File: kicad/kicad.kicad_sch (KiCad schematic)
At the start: 7 parts, among them J1 Screw_Terminal_01x14, U1 Pico

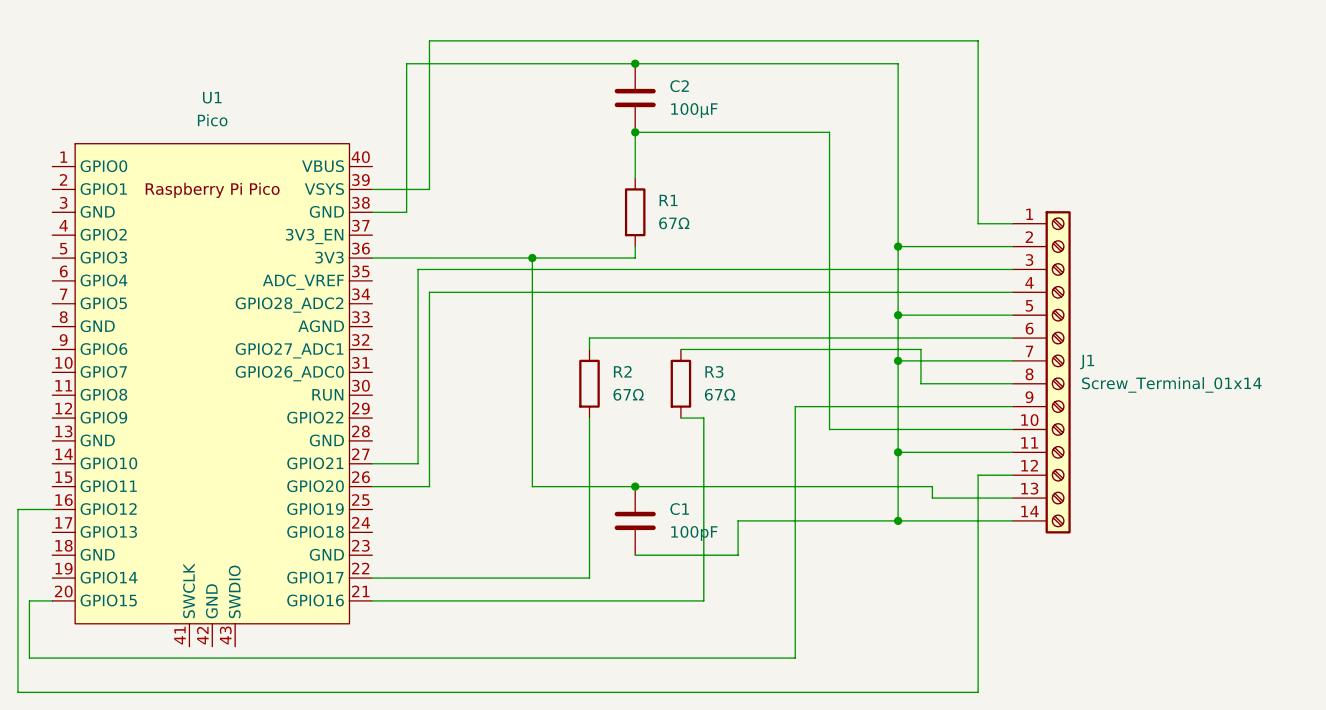
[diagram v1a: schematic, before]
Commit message: new PCB layout
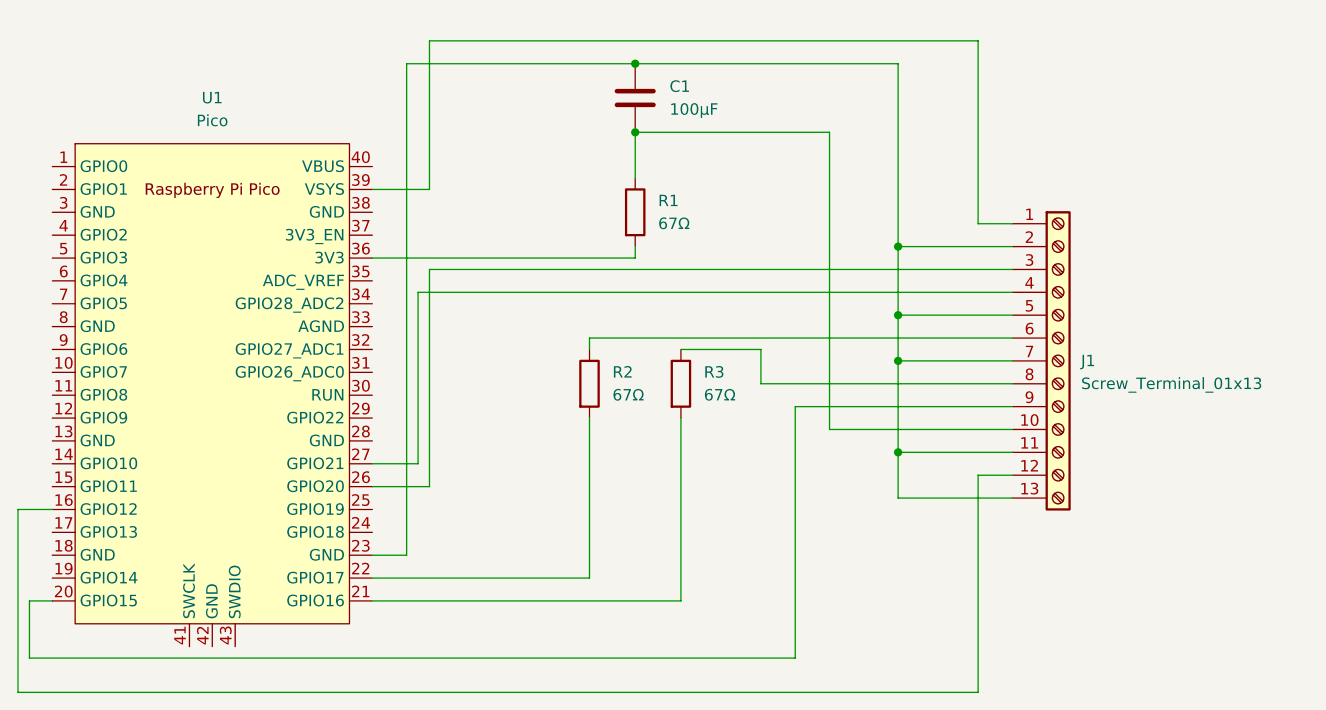
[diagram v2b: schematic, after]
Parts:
- removed C1: 100pF, Capacitor_THT:C_Disc_D7.0mm_W2.5mm_P5.00mm, symbol Device:C
- J1: value Screw_Terminal_01x14 -> Screw_Terminal_01x13
- renumbered C2 to C1
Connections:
- net at R1.2, U1.36 (3V3): no longer J1.13 (Pin_13)
- net at C1.1, J1.11 (Pin_11), J1.2 (Pin_2)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: now also J1.13 (Pin_13), U1.23 (GND); no longer J1.14 (Pin_14), U1.38 (GND)
- net at U1.26 (GPIO20): now also J1.3 (Pin_3); no longer J1.4 (Pin_4)
- net at U1.27 (GPIO21): now also J1.4 (Pin_4); no longer J1.3 (Pin_3)
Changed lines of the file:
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@@
   (junction (at 217.17 88.9) (diameter 0) (color 0 0 0 0)
   )
-  (junction (at 217.17 106.68) (diameter 0) (color 0 0 0 0)
-  )
   (junction (at 217.17 83.82) (diameter 0) (color 0 0 0 0)
   )
-  (junction (at 176.53 77.47) (diameter 0) (color 0 0 0 0)
-  )
   (junction (at 217.17 99.06) (diameter 0) (color 0 0 0 0)
   )
   (junction (at 187.96 55.88) (diameter 0) (color 0 0 0 0)
   )
-  (junction (at 187.96 102.87) (diameter 0) (color 0 0 0 0)
-  )
   (junction (at 217.17 76.2) (diameter 0) (color 0 0 0 0)
   )
@@
     (stroke (width 0) (type default))
   )
-  (wire (pts (xy 220.98 102.87) (xy 187.96 102.87))
-    (stroke (width 0) (type default))
-  )
-  (wire (pts (xy 193.04 87.63) (xy 219.71 87.63))
-    (stroke (width 0) (type default))
-  )
-  (wire (pts (xy 220.98 104.14) (xy 220.98 102.87))
+  (wire (pts (xy 162.56 55.88) (xy 162.56 110.49))
     (stroke (width 0) (type default))
   )
@@
     (stroke (width 0) (type default))
   )
+  (wire (pts (xy 217.17 99.06) (xy 217.17 104.14))
+    (stroke (width 0) (type default))
+  )
+  (wire (pts (xy 158.75 115.57) (xy 193.04 115.57))
+    (stroke (width 0) (type default))
+  )
+  (wire (pts (xy 201.93 87.63) (xy 193.04 87.63))
+    (stroke (width 0) (type default))
+  )
   (wire (pts (xy 182.88 87.63) (xy 182.88 86.36))
     (stroke (width 0) (type default))
@@
     (stroke (width 0) (type default))
   )
+  (wire (pts (xy 165.1 78.74) (xy 229.87 78.74))
+    (stroke (width 0) (type default))
+  )
   (wire (pts (xy 120.65 121.92) (xy 205.74 121.92))
     (stroke (width 0) (type default))
   )
-  (wire (pts (xy 199.39 110.49) (xy 187.96 110.49))
-    (stroke (width 0) (type default))
-  )
-  (wire (pts (xy 217.17 99.06) (xy 217.17 106.68))
-    (stroke (width 0) (type default))
-  )
-  (wire (pts (xy 176.53 102.87) (xy 187.96 102.87))
+  (wire (pts (xy 217.17 104.14) (xy 229.87 104.14))
     (stroke (width 0) (type default))
   )
@@
     (stroke (width 0) (type default))
   )
-  (wire (pts (xy 158.75 77.47) (xy 176.53 77.47))
+  (wire (pts (xy 158.75 77.47) (xy 187.96 77.47))
     (stroke (width 0) (type default))
   )
@@
     (stroke (width 0) (type default))
   )
-  (wire (pts (xy 195.58 95.25) (xy 193.04 95.25))
-    (stroke (width 0) (type default))
-  )
   (wire (pts (xy 158.75 100.33) (xy 163.83 100.33))
     (stroke (width 0) (type default))
@@
     (stroke (width 0) (type default))
   )
-  (wire (pts (xy 176.53 77.47) (xy 176.53 102.87))
-    (stroke (width 0) (type default))
-  )
   (wire (pts (xy 119.38 125.73) (xy 119.38 105.41))
     (stroke (width 0) (type default))
   )
-  (wire (pts (xy 176.53 77.47) (xy 187.96 77.47))
+  (wire (pts (xy 163.83 100.33) (xy 163.83 81.28))
+    (stroke (width 0) (type default))
+  )
+  (wire (pts (xy 162.56 110.49) (xy 158.75 110.49))
     (stroke (width 0) (type default))
   )
@@
     (stroke (width 0) (type default))
   )
-  (wire (pts (xy 158.75 115.57) (xy 195.58 115.57))
-    (stroke (width 0) (type default))
-  )
-  (wire (pts (xy 229.87 106.68) (xy 217.17 106.68))
-    (stroke (width 0) (type default))
-  )
   (wire (pts (xy 205.74 93.98) (xy 205.74 121.92))
     (stroke (width 0) (type default))
@@
     (stroke (width 0) (type default))
   )
-  (wire (pts (xy 162.56 72.39) (xy 162.56 55.88))
-    (stroke (width 0) (type default))
-  )
-  (wire (pts (xy 229.87 104.14) (xy 220.98 104.14))
-    (stroke (width 0) (type default))
-  )
   (wire (pts (xy 182.88 86.36) (xy 229.87 86.36))
     (stroke (width 0) (type default))
@@
     (stroke (width 0) (type default))
   )
-  (wire (pts (xy 199.39 106.68) (xy 199.39 110.49))
-    (stroke (width 0) (type default))
-  )
-  (wire (pts (xy 219.71 91.44) (xy 229.87 91.44))
+  (wire (pts (xy 201.93 91.44) (xy 229.87 91.44))
     (stroke (width 0) (type default))
   )
@@
     (stroke (width 0) (type default))
   )
-  (wire (pts (xy 165.1 81.28) (xy 229.87 81.28))
-    (stroke (width 0) (type default))
-  )
   (wire (pts (xy 119.38 125.73) (xy 226.06 125.73))
     (stroke (width 0) (type default))
   )
-  (wire (pts (xy 163.83 78.74) (xy 229.87 78.74))
-    (stroke (width 0) (type default))
-  )
   (wire (pts (xy 187.96 55.88) (xy 217.17 55.88))
     (stroke (width 0) (type default))
   )
-  (wire (pts (xy 163.83 100.33) (xy 163.83 78.74))
-    (stroke (width 0) (type default))
-  )
-  (wire (pts (xy 195.58 115.57) (xy 195.58 95.25))
-    (stroke (width 0) (type default))
-  )
-  (wire (pts (xy 217.17 106.68) (xy 199.39 106.68))
+  (wire (pts (xy 201.93 91.44) (xy 201.93 87.63))
     (stroke (width 0) (type default))
   )
@@
     (stroke (width 0) (type default))
   )
-  (wire (pts (xy 219.71 87.63) (xy 219.71 91.44))
+  (wire (pts (xy 163.83 81.28) (xy 229.87 81.28))
     (stroke (width 0) (type default))
   )
@@
     (stroke (width 0) (type default))
   )
-  (wire (pts (xy 165.1 102.87) (xy 165.1 81.28))
+  (wire (pts (xy 165.1 78.74) (xy 165.1 102.87))
     (stroke (width 0) (type default))
   )
@@
     (stroke (width 0) (type default))
   )
-  (wire (pts (xy 158.75 72.39) (xy 162.56 72.39))
+  (wire (pts (xy 193.04 115.57) (xy 193.04 95.25))
     (stroke (width 0) (type default))
   )
@@
         (path "/54f8256b-8f68-4e32-9f02-deb8f594533d"
           (reference "R1") (unit 1)
-        )
-      )
-    )
-  )
-  (symbol (lib_id "Device:C") (at 187.96 106.68 0) (unit 1)
-    (in_bom yes) (on_board yes) (dnp no) (fields_autoplaced)
-    (property "Reference" "C1" (at 191.77 105.41 0)
-      (effects (font (size 1.27 1.27)) (justify left))
-    )
-    (property "Value" "100pF" (at 191.77 107.95 0)
-      (effects (font (size 1.27 1.27)) (justify left))
-    )
-    (property "Footprint" "Capacitor_THT:C_Disc_D7.0mm_W2.5mm_P5.00mm" (at 188.9252 110.49 0)
-      (effects (font (size 1.27 1.27)) hide)
-    )
-    (property "Datasheet" "~" (at 187.96 106.68 0)
-      (effects (font (size 1.27 1.27)) hide)
-    )
-    (pin "1")
-    (pin "2")
-    (instances
-      (project "kicad"
-        (path "/54f8256b-8f68-4e32-9f02-deb8f594533d"
-          (reference "C1") (unit 1)
         )
       )
@@
   (symbol (lib_id "Device:C") (at 187.96 59.69 0) (unit 1)
     (in_bom yes) (on_board yes) (dnp no) (fields_autoplaced)
-    (property "Reference" "C2" (at 191.77 58.42 0)
+    (property "Reference" "C1" (at 191.77 58.42 0)
       (effects (font (size 1.27 1.27)) (justify left))
     )
@@
       (project "kicad"
         (path "/54f8256b-8f68-4e32-9f02-deb8f594533d"
-          (reference "C2") (unit 1)
+          (reference "C1") (unit 1)
         )
       )
@@
       (effects (font (size 1.27 1.27)) (justify left))
     )
-    (property "Value" "Screw_Terminal_01x14" (at 237.49 91.44 0)
+    (property "Value" "Screw_Terminal_01x13" (at 237.49 91.44 0)
       (effects (font (size 1.27 1.27)) (justify left))
     )
@@
     )
     (pin "8")
-    (pin "14")
     (pin "5")
     (pin "3")

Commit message: add external pullup resistor
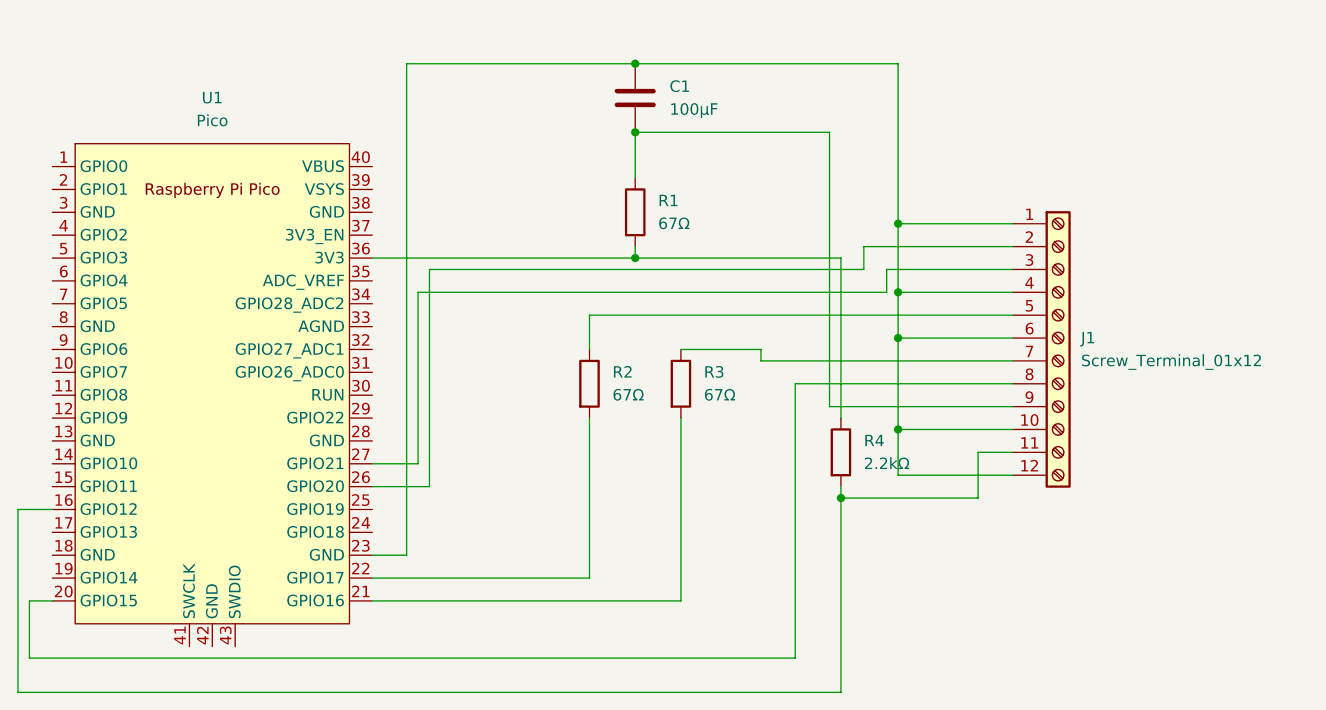
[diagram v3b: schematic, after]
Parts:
- removed J1: Screw_Terminal_01x13, Library:terminal_block_14, symbol Connector:Screw_Terminal_01x14
- added J1: Screw_Terminal_01x12, Library:terminal_block_12, symbol Connector:Screw_Terminal_01x12
- added R4: 2.2kΩ, Resistor_THT:R_Axial_DIN0207_L6.3mm_D2.5mm_P10.16mm_Horizontal, symbol Device:R
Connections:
- net at R3.1: now also J1.7 (Pin_7)
- net at R2.1: now also J1.5 (Pin_5)
- net at C1.2, R1.1: now also J1.9 (Pin_9)
- net at R1.2, U1.36 (3V3): now also R4.1
- net at U1.16 (GPIO12): now also J1.11 (Pin_11), R4.2
- net at U1.20 (GPIO15): now also J1.8 (Pin_8)
- net at C1.1, U1.23 (GND): now also J1.1 (Pin_1), J1.10 (Pin_10), J1.12 (Pin_12), J1.4 (Pin_4), J1.6 (Pin_6)
- net at U1.26 (GPIO20): now also J1.2 (Pin_2)
- net at U1.27 (GPIO21): now also J1.3 (Pin_3)
